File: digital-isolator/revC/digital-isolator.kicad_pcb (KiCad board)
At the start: 2 copper layers, 43.2 x 35.6 mm, 16 parts, among them P1 USB_OTG, P2 Mezzanine-Receptacle, P3 CONN_01X01, P4 CONN_01X01, P5 CONN_01X01, P6 CONN_01X01, U1 ADUM3160

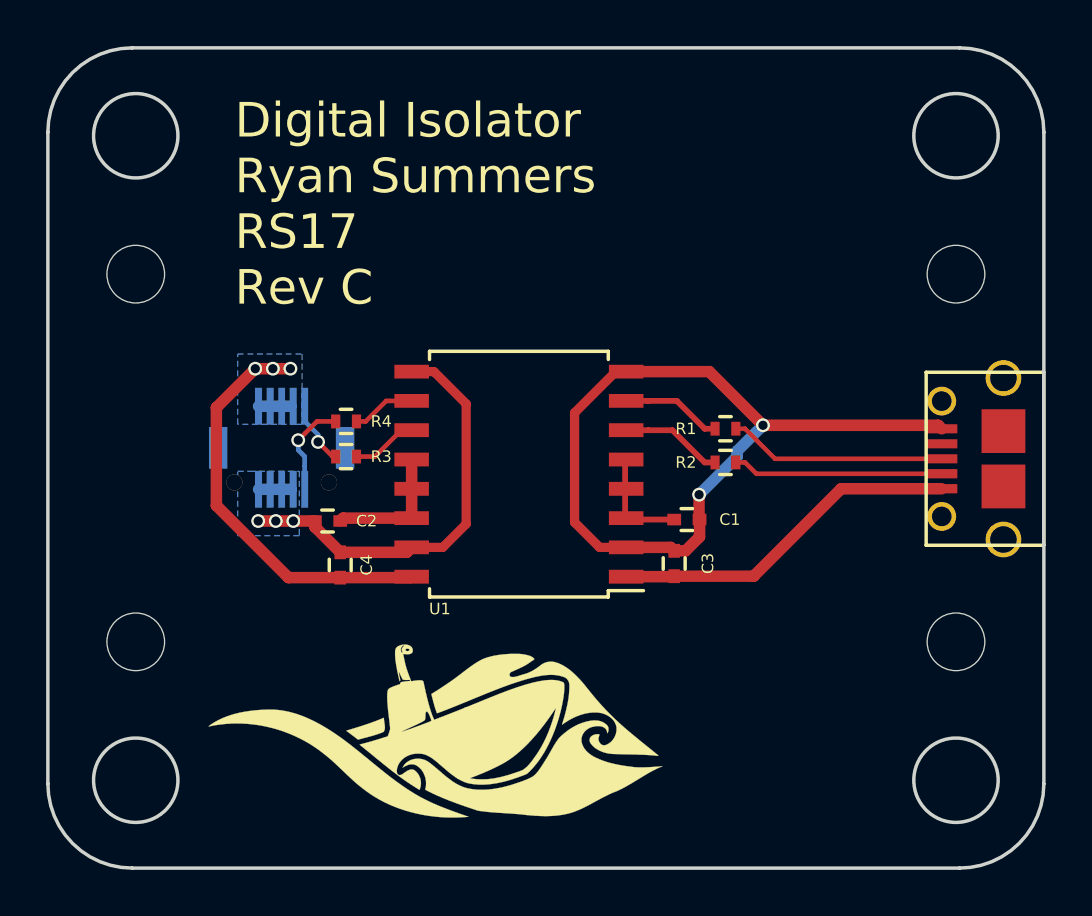
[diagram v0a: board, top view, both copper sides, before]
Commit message: converted edge-cut mounting holes to KiCAD components
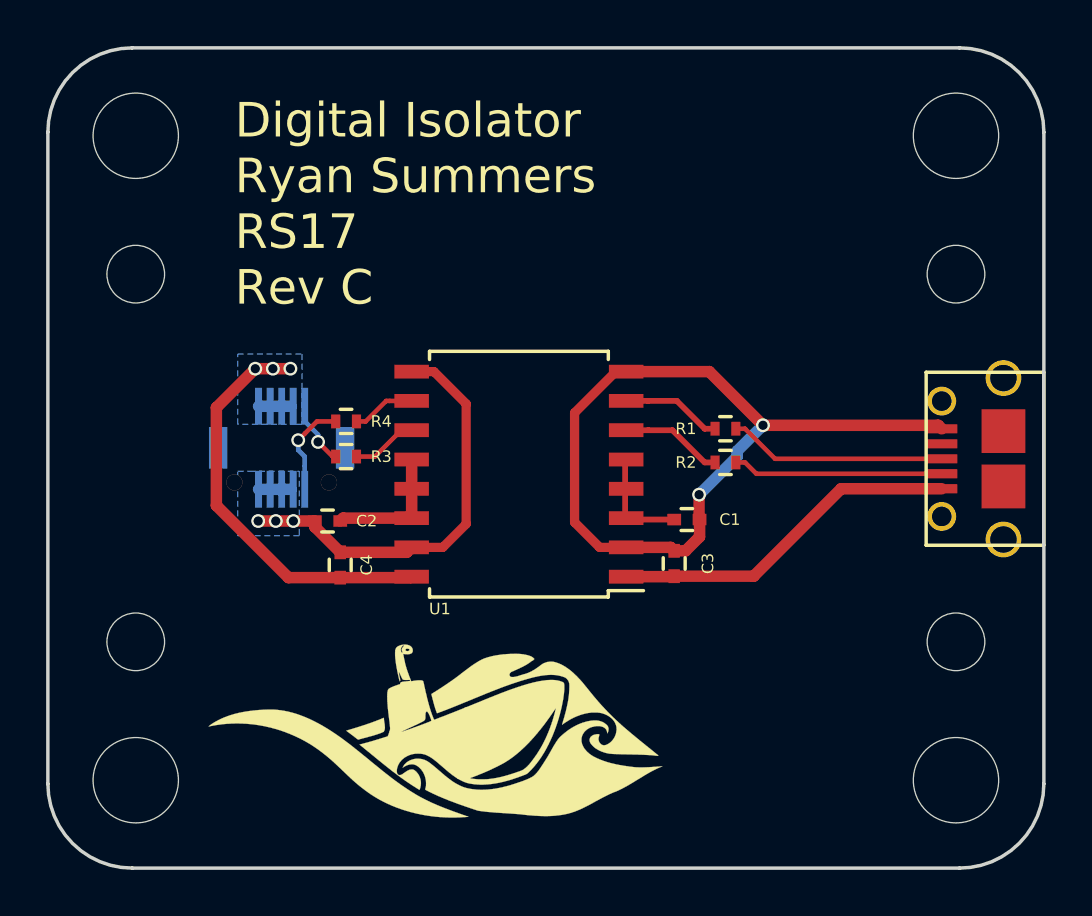
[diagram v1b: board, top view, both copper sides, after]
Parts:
- added REF**: MountingHole_3.7mm, Mounting_Holes:MountingHole_3.7mm, F.Cu at (147.9, 86.5)
- added REF**: MountingHole_3.7mm, Mounting_Holes:MountingHole_3.7mm, F.Cu at (147.9, 114.5)
- added REF**: MountingHole_3.7mm, Mounting_Holes:MountingHole_3.7mm, F.Cu at (112.3, 114.5)
- added REF**: MountingHole_3.7mm, Mounting_Holes:MountingHole_3.7mm, F.Cu at (112.3, 86.5)
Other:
- outline, holes or cut-outs redrawn
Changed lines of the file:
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@@
 (kicad_pcb (version 4) (host pcbnew 4.0.5-e0-6337~49~ubuntu16.04.1)
   (general
-    (links 0)
+    (links 32)
     (no_connects 0)
     (area 108.459199 82.663203 151.789201 118.373205)
     (thickness 1.6)
-    (drawings 13)
+    (drawings 9)
     (tracks 103)
     (zones 0)
-    (modules 16)
+    (modules 20)
     (nets 15)
   )
@@
     (uvia_dia 0.3)
     (uvia_drill 0.1)
+  )
+  (module Mounting_Holes:MountingHole_3.7mm (layer F.Cu)
+    (at 147.9042 86.548204)
+    (descr "Mounting Hole 3.7mm, no annular")
+    (tags "mounting hole 3.7mm no annular")
+    (fp_text reference REF** (at 0 -4.7) (layer F.SilkS) hide
+      (effects (font (size 1 1) (thickness 0.15)))
+    )
+    (fp_text value MountingHole_3.7mm (at 0 4.7) (layer F.Fab)
+      (effects (font (size 1 1) (thickness 0.15)))
+    )
+    (fp_circle (center 0 0) (end 3.7 0) (layer Cmts.User) (width 0.15))
+    (fp_circle (center 0 0) (end 3.95 0) (layer F.CrtYd) (width 0.05))
+    (pad 1 np_thru_hole circle (at 0 0) (size 3.7 3.7) (drill 3.7) (layers *.Cu *.Mask))
+  )
+  (module Mounting_Holes:MountingHole_3.7mm (layer F.Cu)
+    (at 147.9042 114.488204)
+    (descr "Mounting Hole 3.7mm, no annular")
+    (tags "mounting hole 3.7mm no annular")
+    (fp_text reference REF** (at 0 -4.7) (layer F.SilkS) hide
+      (effects (font (size 1 1) (thickness 0.15)))
+    )
+    (fp_text value MountingHole_3.7mm (at 0 4.7) (layer F.Fab)
+      (effects (font (size 1 1) (thickness 0.15)))
+    )
+    (fp_circle (center 0 0) (end 3.7 0) (layer Cmts.User) (width 0.15))
+    (fp_circle (center 0 0) (end 3.95 0) (layer F.CrtYd) (width 0.05))
+    (pad 1 np_thru_hole circle (at 0 0) (size 3.7 3.7) (drill 3.7) (layers *.Cu *.Mask))
+  )
+  (module Mounting_Holes:MountingHole_3.7mm (layer F.Cu)
+    (at 112.3442 114.488204)
+    (descr "Mounting Hole 3.7mm, no annular")
+    (tags "mounting hole 3.7mm no annular")
+    (fp_text reference REF** (at 0 -4.7) (layer F.SilkS) hide
+      (effects (font (size 1 1) (thickness 0.15)))
+    )
+    (fp_text value MountingHole_3.7mm (at 0 4.7) (layer F.Fab)
+      (effects (font (size 1 1) (thickness 0.15)))
+    )
+    (fp_circle (center 0 0) (end 3.7 0) (layer Cmts.User) (width 0.15))
+    (fp_circle (center 0 0) (end 3.95 0) (layer F.CrtYd) (width 0.05))
+    (pad 1 np_thru_hole circle (at 0 0) (size 3.7 3.7) (drill 3.7) (layers *.Cu *.Mask))
   )
   (module Capacitors_SMD:C_0402 (layer F.Cu)
@@
       (xy -2.376168 -0.816) (xy -2.374012 -0.812192)) (layer F.SilkS) (width 0.01))
   )
+  (module Mounting_Holes:MountingHole_3.7mm (layer F.Cu)
+    (at 112.3442 86.548204)
+    (descr "Mounting Hole 3.7mm, no annular")
+    (tags "mounting hole 3.7mm no annular")
+    (fp_text reference REF** (at 0 -4.7) (layer F.SilkS) hide
+      (effects (font (size 1 1) (thickness 0.15)))
+    )
+    (fp_text value MountingHole_3.7mm (at 0 4.7) (layer F.Fab)
+      (effects (font (size 1 1) (thickness 0.15)))
+    )
+    (fp_circle (center 0 0) (end 3.7 0) (layer Cmts.User) (width 0.15))
+    (fp_circle (center 0 0) (end 3.95 0) (layer F.CrtYd) (width 0.05))
+    (pad 1 np_thru_hole circle (at 0 0) (size 3.7 3.7) (drill 3.7) (layers *.Cu *.Mask))
+  )
   (gr_line (start 151.7142 114.640604) (end 151.7142 86.395804) (layer Edge.Cuts) (width 0.15))
   (gr_line (start 148.0566 82.738204) (end 112.1918 82.738204) (layer Edge.Cuts) (width 0.15))
-  (gr_circle (center 147.9042 86.548204) (end 149.733 86.548204) (layer Edge.Cuts) (width 0.15))
-  (gr_circle (center 147.9042 114.488204) (end 149.733 114.488204) (layer Edge.Cuts) (width 0.15))
   (gr_arc (start 112.1918 86.395804) (end 112.1918 82.738204) (angle -90) (layer Edge.Cuts) (width 0.15))
   (gr_arc (start 112.1918 114.640604) (end 108.5342 114.640604) (angle -90) (layer Edge.Cuts) (width 0.15))
@@
   (gr_arc (start 148.0566 114.640604) (end 148.0566 118.298204) (angle -89.9) (layer Edge.Cuts) (width 0.15))
   (gr_arc (start 148.0566 86.395804) (end 151.7142 86.395804) (angle -90) (layer Edge.Cuts) (width 0.15))
-  (gr_circle (center 112.3442 86.548204) (end 114.173 86.548204) (layer Edge.Cuts) (width 0.15))
-  (gr_circle (center 112.3442 114.488204) (end 114.173 114.488204) (layer Edge.Cuts) (width 0.15))
   (gr_text "Digital Isolator\nRyan Summers\nRS17\nRev C" (at 116.6368 89.5096) (layer F.SilkS)
     (effects (font (size 1.5 1.5) (thickness 0.3)) (justify left))
